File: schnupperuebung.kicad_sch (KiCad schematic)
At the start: 5 parts, among them J3 USB_C_Receptacle_PowerOnly_6P

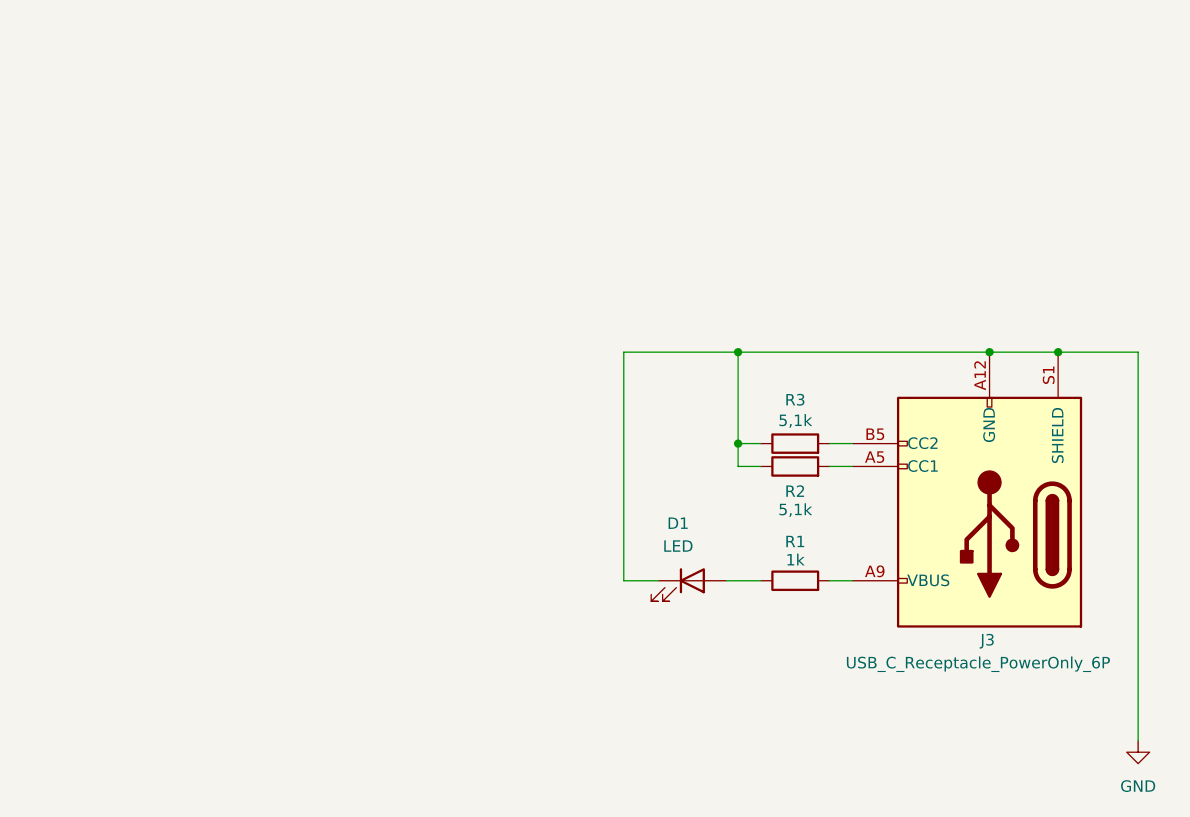
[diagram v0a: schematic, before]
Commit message: Updated Footprint & Created pics
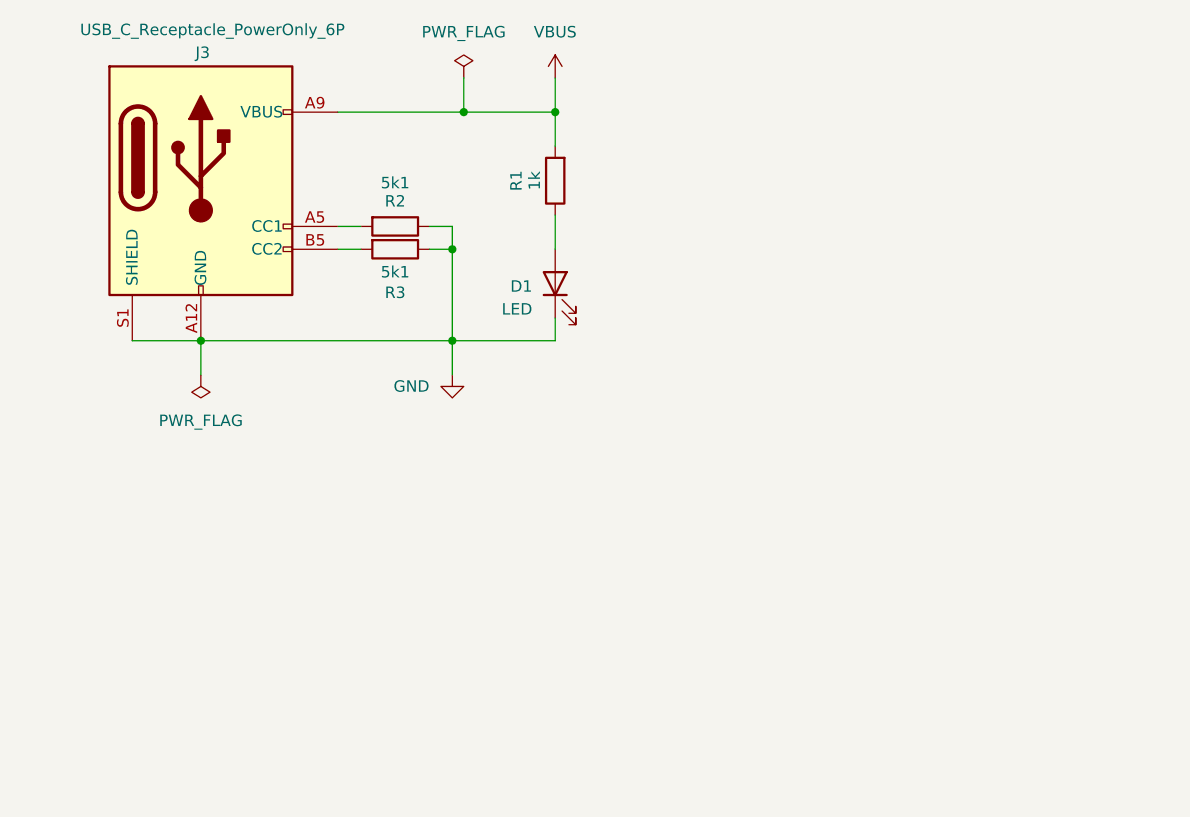
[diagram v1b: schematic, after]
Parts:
- R1: footprint Resistor_THT:R_Axial_DIN0204_L3.6mm_D1.6mm_P7.62mm_Horizontal -> Resistor_THT:R_Axial_DIN0207_L6.3mm_D2.5mm_P15.24mm_Horizontal
- R2, R3: value 5,1k -> 5k1
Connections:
- net VBUS: now reaches J3.A9 (VBUS), J3.B9 (VBUS), R1.2
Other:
- company: (none) -> HTL-Steyr
- title: (none) -> Schnupperübung 1LED 1R USB-C
- moved on the sheet: D1, J3, R1, R2, R3
